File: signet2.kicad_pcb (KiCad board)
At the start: 6 copper layers, 16 x 28.5 mm, 57 parts, among them IC1 THGBMHG8C2LBAIL, J1 480372200, J3 Conn_01x02_Male, SW1 EVQ_PLDA15, U1 LDFM33PUR, U2 STM32F733IEKx, U3 USBULC6-2M6, Y1 ABM10-167-12.000MHZ-T3

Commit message: Thermal and mechanical improvements
- Change user header to round through hole pads
- Remove most GND pour areas around user header GND pin so it is easier
to heat and solder/desolder
- Tighten fit of USB connector mounting slots
- Reduce the size of the increased thickness area at USB connector
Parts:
- added J10: Conn_01x01_Male, signet2:TestPoint_Pad_1.5x1.5mm, B.Cu at (93.3, 118.8)
- added J11: Conn_01x01_Male, signet2:TestPoint_Pad_1.5x1.5mm, B.Cu at (93.3, 116.8)
- added J2: Conn_01x01_Male, signet2:TestPoint_Pad_1.5x1.5mm, B.Cu at (106.8, 113.9)
- added J4: Conn_01x01_Male, signet2:TestPoint_Pad_1.5x1.5mm, B.Cu at (93.3, 124.8)
- added J6: Conn_01x01_Male, signet2:TestPoint_Pad_1.5x1.5mm, B.Cu at (98.1, 117.5)
- added J7: Conn_01x01_Male, signet2:TestPoint_Pad_1.5x1.5mm, B.Cu at (93.3, 126.8)
- added J8: Conn_01x01_Male, signet2:TestPoint_Pad_1.5x1.5mm, B.Cu at (93.3, 122.8)
- added J9: Conn_01x01_Male, signet2:TestPoint_Pad_1.5x1.5mm, B.Cu at (93.3, 120.8)
- J3: value Conn_01x02_Male -> Conn_01x01_Male; footprint signet2:signet-hc-connector -> signet2:TestPoint_Pad_1.5x1.5mm
- moved J3 13.6 mm to (106.8, 116.0), turned to 0 degrees
- moved R17 2.09 mm to (94.9, 125.7), turned to 90 degrees
- moved R18 1.57 mm to (95.4, 123.7)
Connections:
- J3 pad 1: /NRST -> /SWD_CLK
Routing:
- net /SWD_IO: track 23.3 -> 3.07 mm
- net /SWD_CLK: track 22.5 -> 2.87 mm
- net /NRST: track 17.8 -> 14.9 mm, vias 3 -> 2
- net /BOOTSW: track 2.51 -> 4.79 mm
- net /BOOT0: track 11.3 -> 12.0 mm
- net /GPIO1: track 9.96 -> 10.7 mm
- net VDD: track 39.7 -> 39.6 mm, vias 19 -> 18
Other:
- board size 16 x 28.5 mm -> 16 x 28.3 mm

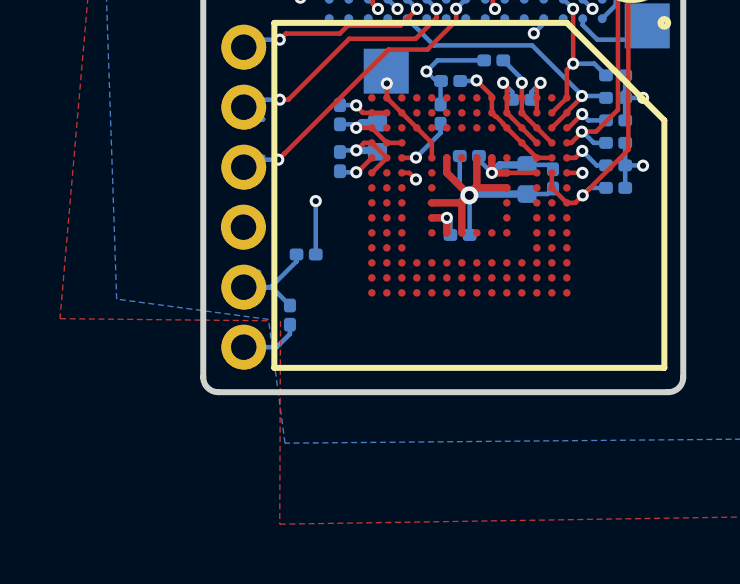
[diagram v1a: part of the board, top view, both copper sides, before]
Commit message: Version 1.22
- Add GND plane pour to GND line through-hole connection
- Change visual layout in schematic (connections are the same)
- Make area sticking out near USB port smaller. Needed to take into
consideration the possible need for the port to be able to bend
slightly down to fit in enclosure. This will depend on the exact PCB
thickness and how the USB port seats on it.
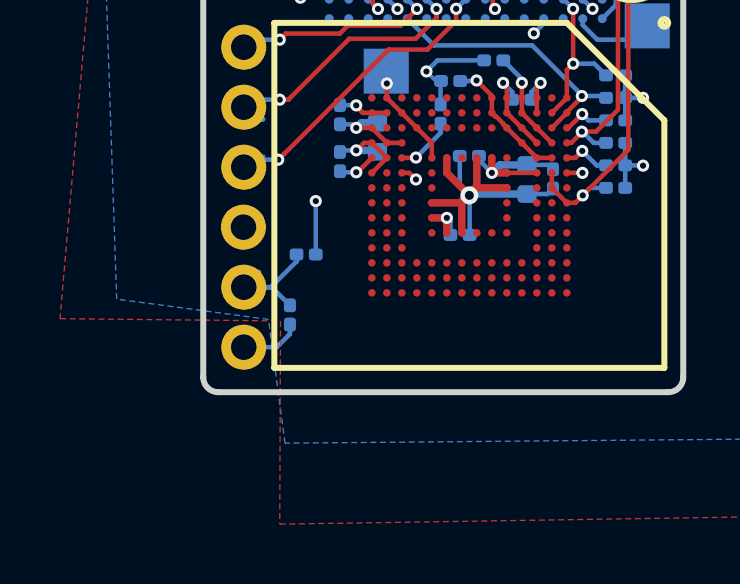
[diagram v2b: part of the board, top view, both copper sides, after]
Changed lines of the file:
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@@
     (4 In4.Cu signal)
     (31 B.Cu signal)
-    (32 B.Adhes user hide)
+    (32 B.Adhes user)
     (33 F.Adhes user hide)
     (34 B.Paste user hide)
-    (35 F.Paste user)
-    (36 B.SilkS user)
+    (35 F.Paste user hide)
+    (36 B.SilkS user hide)
     (37 F.SilkS user hide)
     (38 B.Mask user)
@@
     (aux_axis_origin 100 100)
     (grid_origin 100 99.9)
-    (visible_elements 7FFFF77F)
+    (visible_elements 7FF9F71F)
     (pcbplotparams
       (layerselection 0x010fc_ffffffff)
@@
       (effects (font (size 1 1) (thickness 0.15)) (justify mirror))
     )
-    (pad "" thru_hole circle (at 0 0) (size 1.5 1.5) (drill 0.85) (layers *.Cu *.Mask)
+    (pad 1 thru_hole circle (at 0 0) (size 1.5 1.5) (drill 0.85) (layers *.Cu *.Mask)
       (net 2 GND))
   )
@@
   )
   (module Resistor_SMD:R_0201_0603Metric (layer B.Cu)
-    (at 94.89 125.68 90)
+    (at 94.89 125.675 90)
     (descr "Resistor SMD 0201 (0603 Metric), square (rectangular) end terminal, IPC_7351 nominal, (Body size source: https://www.vishay.com/docs/20052/crcw0201e3.pdf), generated with kicad-footprint-generator")
     (tags resistor)
@@
       (xy -2.549664 -1.91989) (xy -2.469928 -1.911165) (xy -2.400256 -1.919918)) (layer B.SilkS) (width 0.01))
   )
+  (gr_arc (start 107.5 127.75) (end 107.5 128.25) (angle -90) (layer Edge.Cuts) (width 0.2))
+  (gr_line (start 108 106.5) (end 108 127.75) (layer Edge.Cuts) (width 0.2))
   (gr_line (start 105.1 100) (end 107.5 100) (layer Edge.Cuts) (width 0.2))
   (gr_arc (start 105 100) (end 105 99.9) (angle 90) (layer Edge.Cuts) (width 0.2))
@@
   (gr_arc (start 107.5 100.5) (end 107.5 100) (angle 90) (layer Edge.Cuts) (width 0.2))
   (gr_arc (start 92.5 100.5) (end 92.5 100) (angle -90) (layer Edge.Cuts) (width 0.2))
-  (gr_arc (start 107.5 127.75) (end 107.5 128.25) (angle -90) (layer Edge.Cuts) (width 0.2))
   (gr_arc (start 92.5 127.75) (end 92 127.75) (angle -90) (layer Edge.Cuts) (width 0.2))
   (gr_line (start 107 129) (end 107 98) (layer Dwgs.User) (width 0.2))
@@
   (gr_line (start 92 105) (end 93 105) (layer Edge.Cuts) (width 0.2))
   (gr_line (start 92 106.5) (end 93 106.5) (layer Edge.Cuts) (width 0.2))
-  (gr_line (start 108 106.5) (end 108 127.75) (layer Edge.Cuts) (width 0.2))
   (gr_line (start 107.5 128.25) (end 92.5 128.25) (layer Edge.Cuts) (width 0.2))
   (gr_line (start 92 106.5) (end 92 127.75) (layer Edge.Cuts) (width 0.2))
